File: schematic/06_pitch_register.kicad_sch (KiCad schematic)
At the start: 28 parts, among them J201 analog control boundary, J202 logic test header, U221 74HC377, U222 74HC154

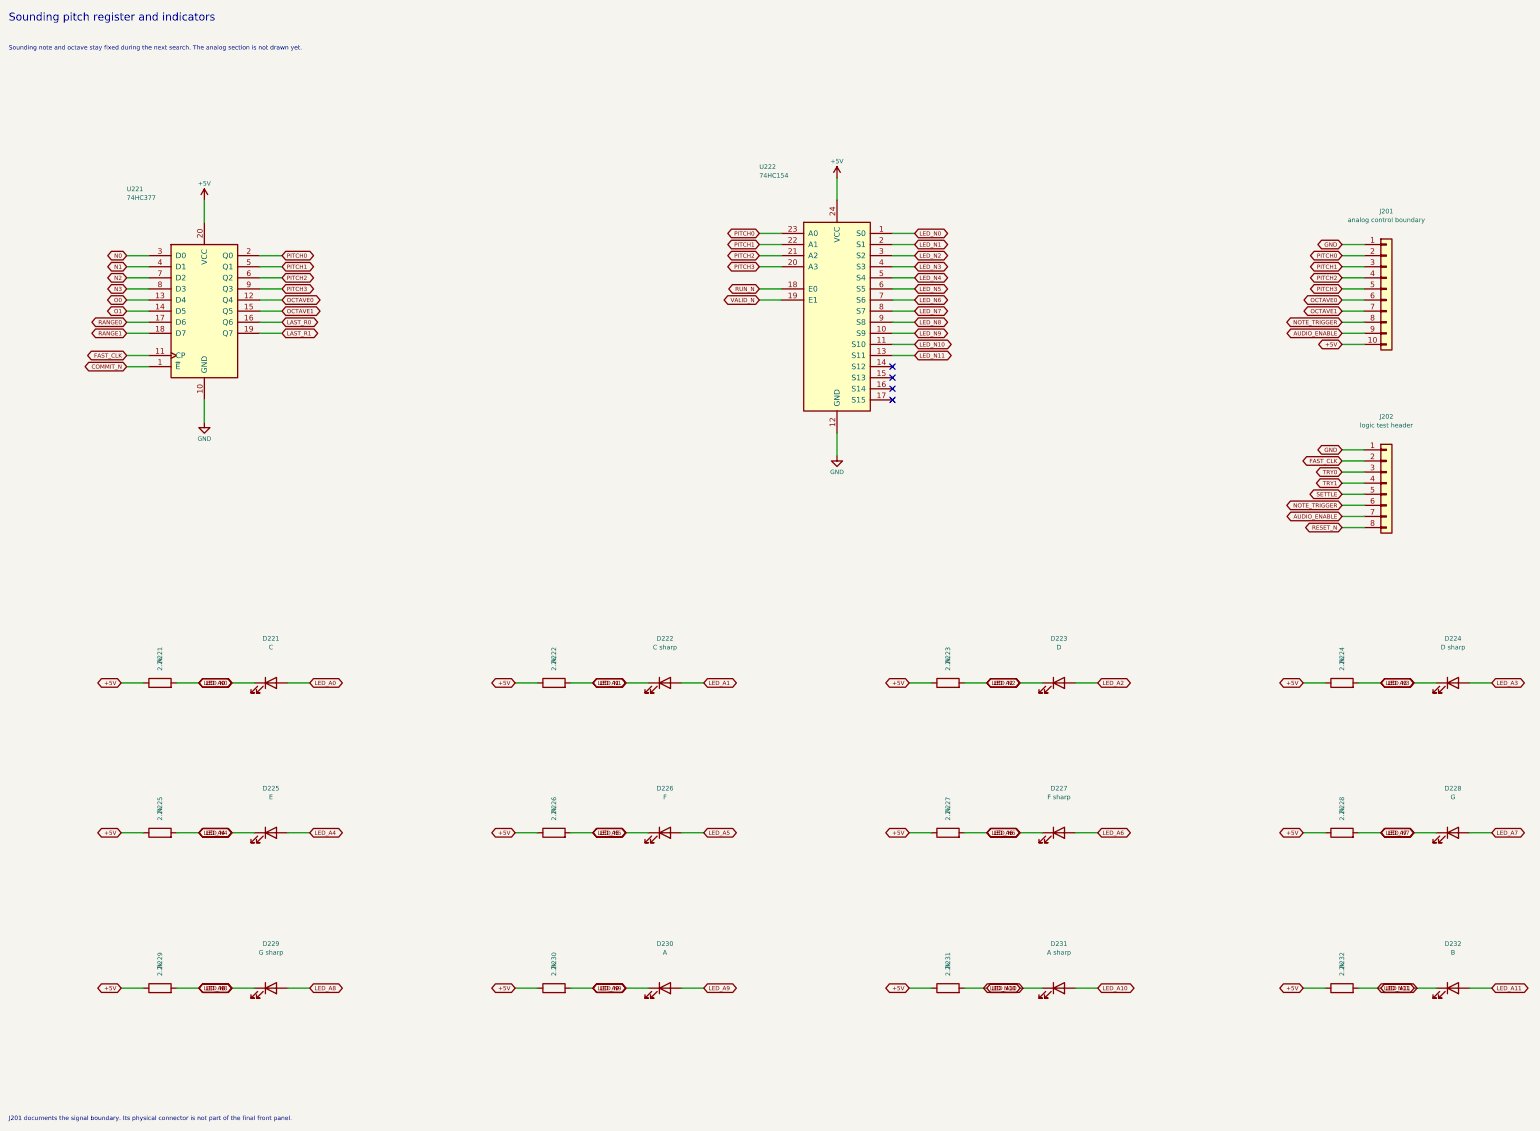
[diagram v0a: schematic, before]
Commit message: add the pitch and sound circuit
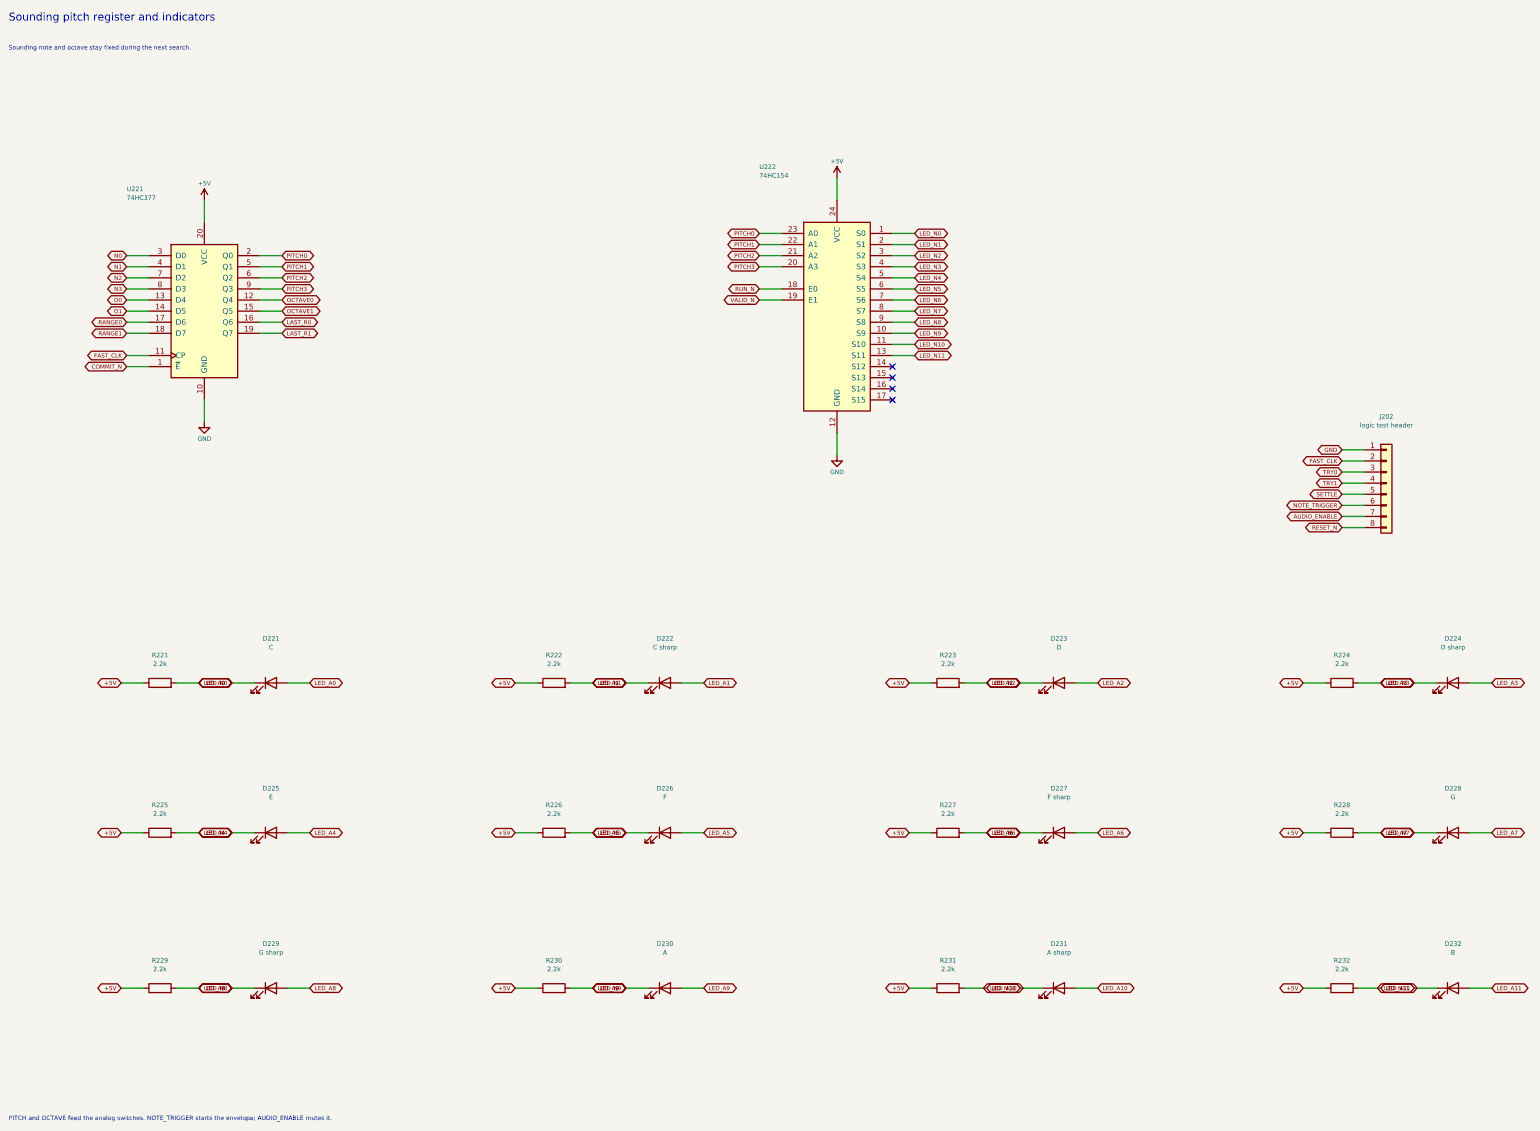
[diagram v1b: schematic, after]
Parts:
- removed J201: analog control boundary, symbol Connector_Generic:Conn_01x10
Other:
- note added: "PITCH and OCTAVE feed the analog switches. NOTE_TRIGGER starts the envelope; AUDIO_ENABLE mutes it."
- note added: "Sounding note and octave stay fixed during the next search."
- note removed: "J201 documents the signal boundary. Its physical connector is not part of the final front panel."
- note removed: "Sounding note and octave stay fixed during the next search. The analog section is not drawn yet."

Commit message: add power supply, rail checks and parts list
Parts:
- U221: MPN (none) -> 74HC377D,653; Manufacturer (none) -> Nexperia; Supplier (none) -> LCSC; Supplier URL (none) -> https://www.lcsc.com/product-detail/C5639.html
- U222: MPN (none) -> 74HC154D,653; Manufacturer (none) -> Nexperia; Supplier (none) -> LCSC; Supplier URL (none) -> https://www.lcsc.com/product-detail/C13758.html
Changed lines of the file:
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@@
       )
     )
-    (property "Datasheet" "http://www.ti.com/lit/gpn/sn74LS377"
+    (property "Datasheet" "https://assets.nexperia.com/documents/data-sheet/74HC_HCT377.pdf"
       (at 46.989999999999995 57.15000000000001 0.0)
       (effects
@@
         )
         (justify left)
+        (hide yes)
+      )
+    )
+    (property "MPN" "74HC377D,653"
+      (at 64.77 85.09 0.0)
+      (effects
+        (font
+          (size 1.0 1.0)
+        )
+        (hide yes)
+      )
+    )
+    (property "Manufacturer" "Nexperia"
+      (at 64.77 85.09 0.0)
+      (effects
+        (font
+          (size 1.0 1.0)
+        )
+        (hide yes)
+      )
+    )
+    (property "Supplier" "LCSC"
+      (at 64.77 85.09 0.0)
+      (effects
+        (font
+          (size 1.0 1.0)
+        )
+        (hide yes)
+      )
+    )
+    (property "Supplier URL" "https://www.lcsc.com/product-detail/C5639.html"
+      (at 64.77 85.09 0.0)
+      (effects
+        (font
+          (size 1.0 1.0)
+        )
         (hide yes)
       )
@@
       )
     )
-    (property "Datasheet" "http://www.ti.com/lit/gpn/sn74LS154"
+    (property "Datasheet" "https://assets.nexperia.com/documents/data-sheet/74HC_HCT154.pdf"
       (at 191.77 52.07000000000001 0.0)
       (effects
@@
         (hide yes)
       )
+    )
+    (property "MPN" "74HC154D,653"
+      (at 209.55 85.09 0.0)
+      (effects
+        (font
+          (size 1.0 1.0)
+        )
+        (hide yes)
+      )
+    )
+    (property "Manufacturer" "Nexperia"
+      (at 209.55 85.09 0.0)
+      (effects
+        (font
+          (size 1.0 1.0)
+        )
+        (hide yes)
+      )
+    )
+    (property "Supplier" "LCSC"
+      (at 209.55 85.09 0.0)
+      (effects
+        (font
+          (size 1.0 1.0)
+        )
+        (hide yes)
+      )
+    )
+    (property "Supplier URL" "https://www.lcsc.com/product-detail/C13758.html"
+      (at 209.55 85.09 0.0)
+      (effects
+        (font
+          (size 1.0 1.0)
+        )
+        (hide yes)
+      )

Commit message: parts and cheaper PCB files
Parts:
- U222: MPN 74HC154D,653 -> CD74HC154M96; Manufacturer Nexperia -> TI; Supplier URL https://www.lcsc.com/product-detail/C13758.html -> https://www.lcsc.com/product-detail/C2832236.html
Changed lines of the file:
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@@
       )
     )
-    (property "MPN" "74HC154D,653"
+    (property "MPN" "CD74HC154M96"
       (at 209.55 85.09 0.0)
       (effects
@@
       )
     )
-    (property "Manufacturer" "Nexperia"
+    (property "Manufacturer" "TI"
       (at 209.55 85.09 0.0)
       (effects
@@
       )
     )
-    (property "Supplier URL" "https://www.lcsc.com/product-detail/C13758.html"
+    (property "Supplier URL" "https://www.lcsc.com/product-detail/C2832236.html"
       (at 209.55 85.09 0.0)
       (effects
